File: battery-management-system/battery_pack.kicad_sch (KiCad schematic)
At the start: 15 parts, among them J1 Conn_01x01, J2 Conn_01x01, J3 Conn_01x01, J4 Conn_01x01, J5 Conn_01x01, J6 Conn_01x01, Q1 DMN3730U, Q2 TJ40S04M3L, Q3 TJ40S04M3L, Q4 DMN3730U

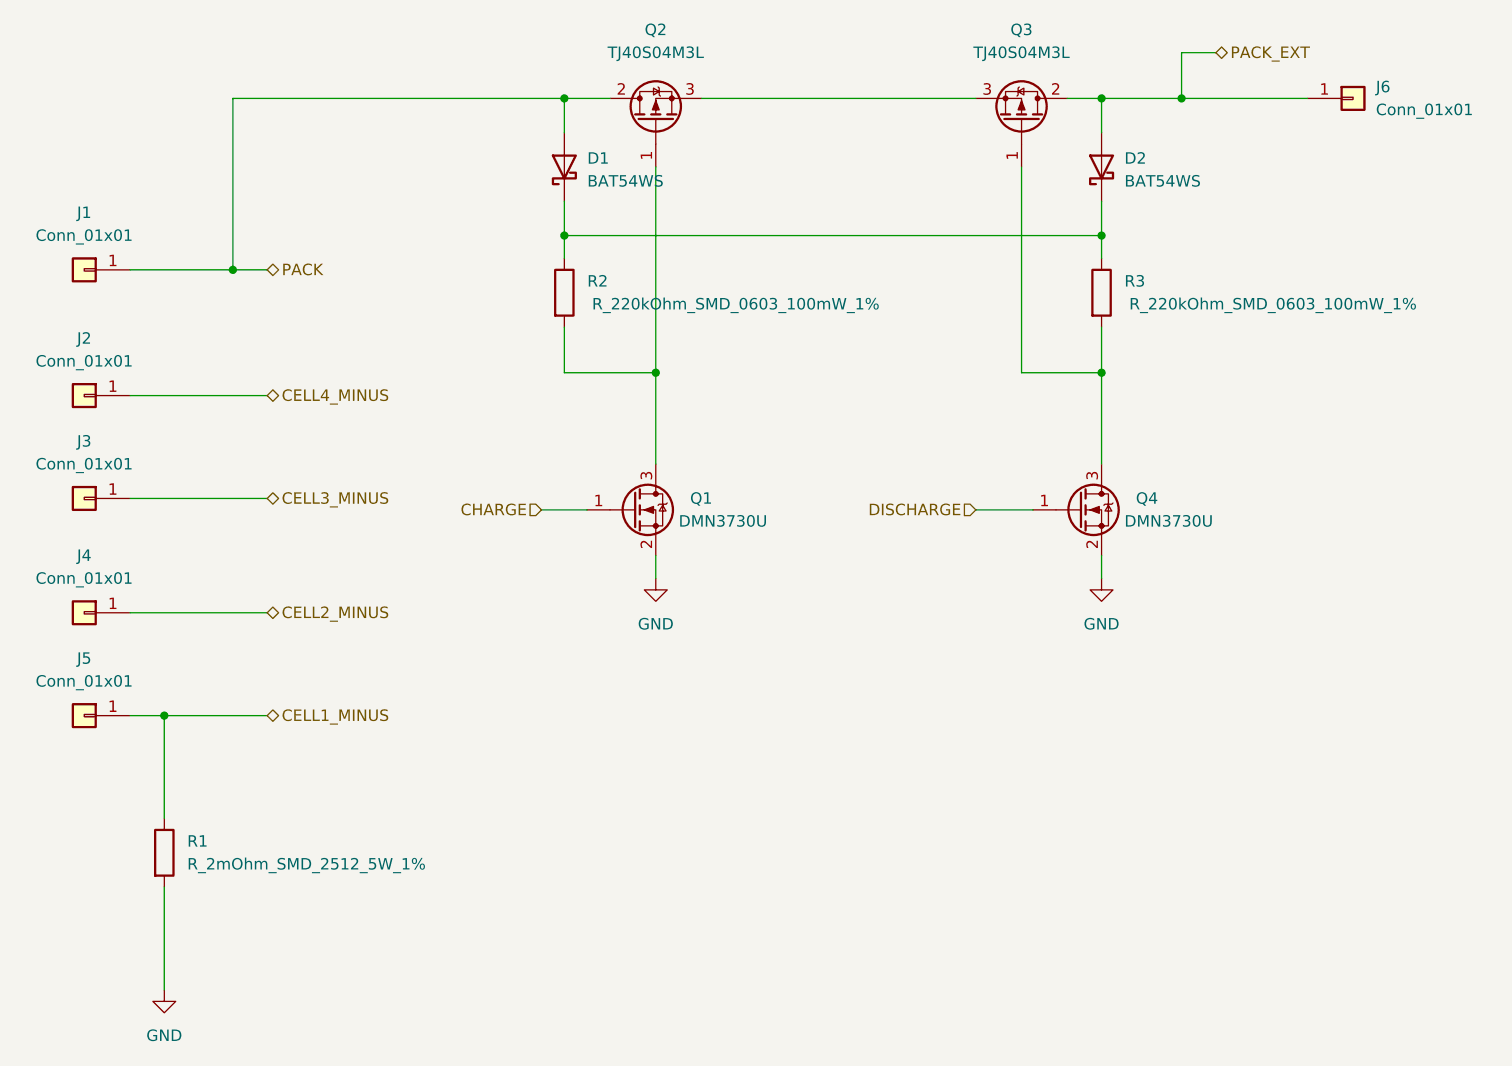
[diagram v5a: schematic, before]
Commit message: use M6 connectors, update symbols
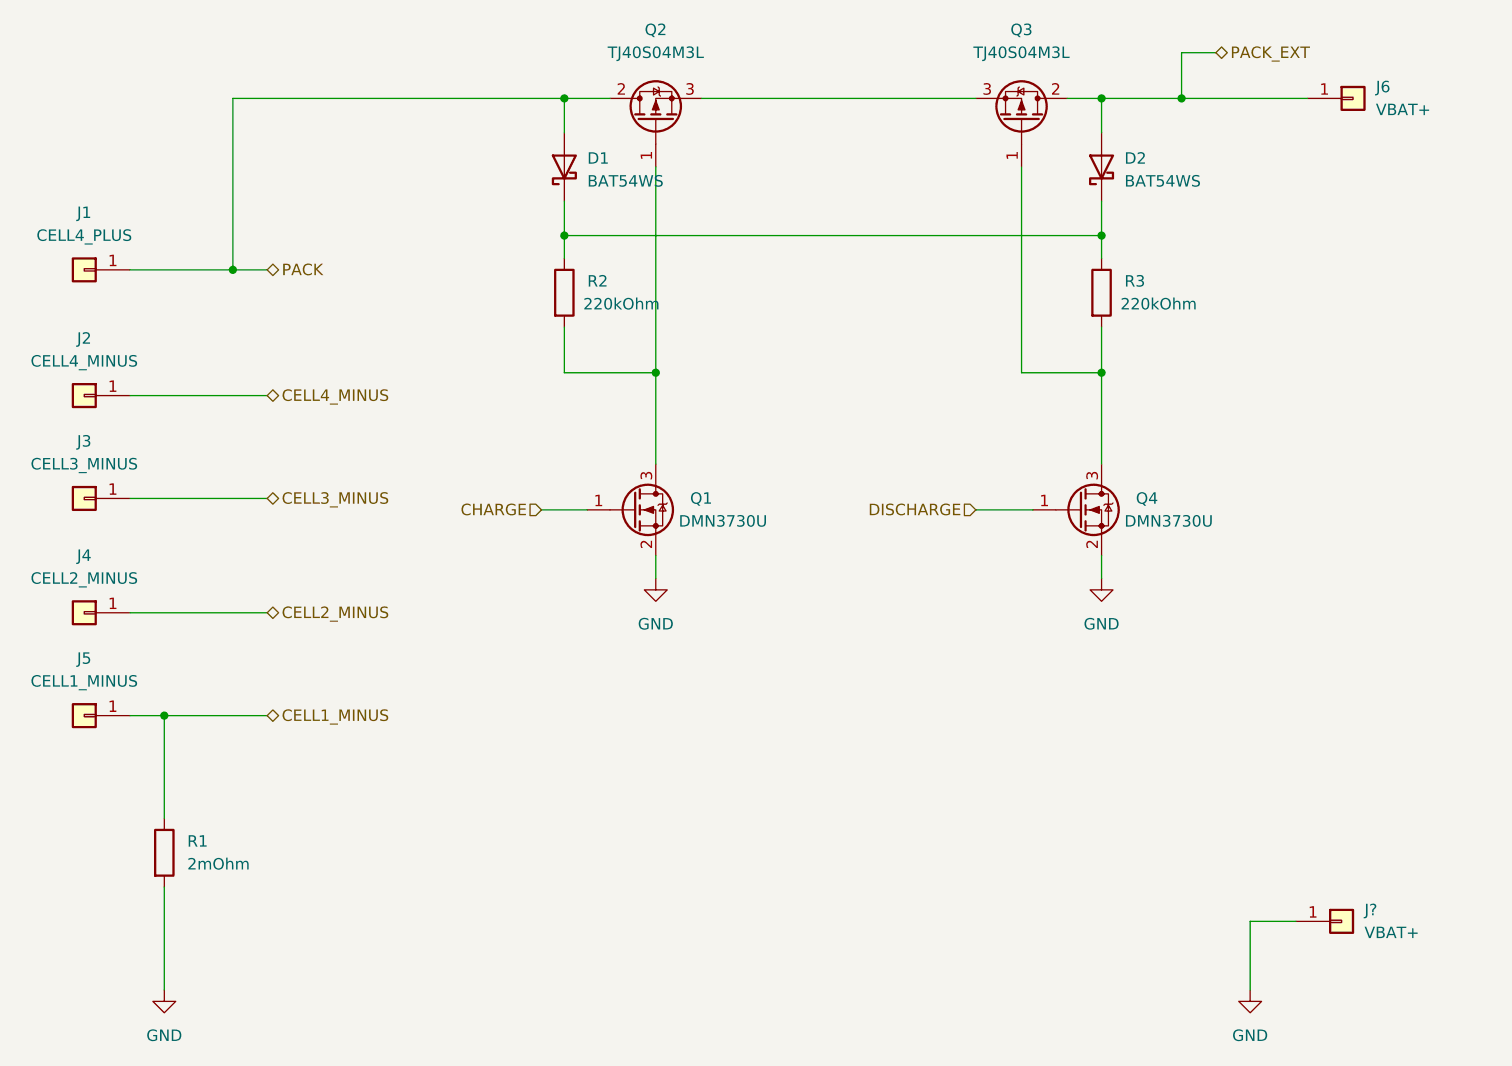
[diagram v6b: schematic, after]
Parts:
- added J?: VBAT+, benediktibk:Connector_M6, symbol benediktibk:Connector_M6
- J1: value Conn_01x01 -> CELL4_PLUS; footprint (none) -> benediktibk:Connector_M6; symbol Connector_Generic:Conn_01x01 -> benediktibk:Connector_M6
- J2: value Conn_01x01 -> CELL4_MINUS; footprint (none) -> benediktibk:Connector_M6; symbol Connector_Generic:Conn_01x01 -> benediktibk:Connector_M6
- J3: value Conn_01x01 -> CELL3_MINUS; footprint (none) -> benediktibk:Connector_M6; symbol Connector_Generic:Conn_01x01 -> benediktibk:Connector_M6
- J4: value Conn_01x01 -> CELL2_MINUS; footprint (none) -> benediktibk:Connector_M6; symbol Connector_Generic:Conn_01x01 -> benediktibk:Connector_M6
- J5: value Conn_01x01 -> CELL1_MINUS; footprint (none) -> benediktibk:Connector_M6; symbol Connector_Generic:Conn_01x01 -> benediktibk:Connector_M6
- J6: value Conn_01x01 -> VBAT+; footprint (none) -> benediktibk:Connector_M6; symbol Connector_Generic:Conn_01x01 -> benediktibk:Connector_M6
- R1: value R_2mOhm_SMD_2512_5W_1% -> 2mOhm; RS order number 231-3683 -> 231-3683
- R2, R3: value R_220kOhm_SMD_0603_100mW_1% -> 220kOhm
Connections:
- net GND: now also J?.1 (Pin_1)
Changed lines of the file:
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@@
+    (stroke (width 0) (type default) (color 0 0 0 0))
+  )
+  (wire (pts (xy 195.58 137.16) (xy 200.66 137.16))
     (stroke (width 0) (type default) (color 0 0 0 0))
   )
@@
   )
   (wire (pts (xy 74.93 114.3) (xy 74.93 125.73))
+    (stroke (width 0) (type default) (color 0 0 0 0))
+  )
+  (wire (pts (xy 195.58 144.78) (xy 195.58 137.16))
     (stroke (width 0) (type default) (color 0 0 0 0))
   )
@@
     (pin "2")
   )
-  (symbol (lib_id "Connector_Generic:Conn_01x01") (at 207.01 45.72 0) (unit 1)
+  (symbol (lib_id "benediktibk:Connector_M6") (at 205.74 137.16 0) (unit 1)
+    (in_bom yes) (on_board yes) (fields_autoplaced)
+    (property "Reference" "J?" (id 0) (at 208.28 135.8899 0)
+      (effects (font (size 1.27 1.27)) (justify left))
+    )
+    (property "Value" "VBAT+" (id 1) (at 208.28 138.4299 0)
+      (effects (font (size 1.27 1.27)) (justify left))
+    )
+    (property "Footprint" "benediktibk:Connector_M6" (id 2) (at 205.994 133.096 0)
+      (effects (font (size 1.27 1.27)) hide)
+    )
+    (property "Datasheet" "~" (id 3) (at 205.74 137.16 0)
+      (effects (font (size 1.27 1.27)) hide)
+    )
+    (property "RS order number" "" (id 4) (at 205.74 137.16 0)
+      (effects (font (size 1.27 1.27)) hide)
+    )
+    (pin "1")
+  )
+  (symbol (lib_id "benediktibk:Connector_M6") (at 207.01 45.72 0) (unit 1)
     (in_bom yes) (on_board yes) (fields_autoplaced)
     (property "Reference" "J6" (id 0) (at 209.55 44.4499 0)
       (effects (font (size 1.27 1.27)) (justify left))
     )
-    (property "Value" "Conn_01x01" (id 1) (at 209.55 46.9899 0)
-      (effects (font (size 1.27 1.27)) (justify left))
-    )
-    (property "Footprint" "" (id 2) (at 207.01 45.72 0)
+    (property "Value" "VBAT+" (id 1) (at 209.55 46.9899 0)
+      (effects (font (size 1.27 1.27)) (justify left))
+    )
+    (property "Footprint" "benediktibk:Connector_M6" (id 2) (at 207.264 41.656 0)
       (effects (font (size 1.27 1.27)) hide)
     )
@@
       (effects (font (size 1.27 1.27)) hide)
     )
-    (pin "1")
-  )
-  (symbol (lib_id "Connector_Generic:Conn_01x01") (at 66.04 90.17 0) (mirror y) (unit 1)
+    (property "RS order number" "" (id 4) (at 207.01 45.72 0)
+      (effects (font (size 1.27 1.27)) hide)
+    )
+    (pin "1")
+  )
+  (symbol (lib_id "benediktibk:Connector_M6") (at 66.04 90.17 0) (mirror y) (unit 1)
     (in_bom yes) (on_board yes) (fields_autoplaced)
     (property "Reference" "J3" (id 0) (at 66.04 83.82 0))
-    (property "Value" "Conn_01x01" (id 1) (at 66.04 86.36 0))
-    (property "Footprint" "" (id 2) (at 66.04 90.17 0)
+    (property "Value" "CELL3_MINUS" (id 1) (at 66.04 86.36 0))
+    (property "Footprint" "benediktibk:Connector_M6" (id 2) (at 65.786 86.106 0)
       (effects (font (size 1.27 1.27)) hide)
     )
     (property "Datasheet" "~" (id 3) (at 66.04 90.17 0)
+      (effects (font (size 1.27 1.27)) hide)
+    )
+    (property "RS order number" "" (id 4) (at 66.04 90.17 0)
       (effects (font (size 1.27 1.27)) hide)
     )
@@
       (effects (font (size 1.27 1.27)) (justify left))
     )
-    (property "Value" "R_220kOhm_SMD_0603_100mW_1%" (id 1) (at 138.43 68.58 0))
+    (property "Value" "220kOhm" (id 1) (at 125.73 68.58 0))
     (property "Footprint" "benediktibk:R_0603_1608Metric_Pad0.98x0.95mm_HandSolder" (id 2) (at 109.22 66.802 90)
       (effects (font (size 1.27 1.27)) hide)
@@
       (effects (font (size 1.27 1.27)) (justify left))
     )
-    (property "Value" "R_2mOhm_SMD_2512_5W_1%" (id 1) (at 77.47 130.8099 0)
+    (property "Value" "2mOhm" (id 1) (at 77.47 130.8099 0)
       (effects (font (size 1.27 1.27)) (justify left))
     )
@@
       (effects (font (size 1.27 1.27)) hide)
     )
-    (property "RS order number" "    231-3683" (id 4) (at 57.15 128.27 0)
+    (property "RS order number" "231-3683" (id 4) (at 57.15 128.27 0)
       (effects (font (size 1.27 1.27)) hide)
     )
@@
       (effects (font (size 1.27 1.27)) (justify left))
     )
-    (property "Value" "R_220kOhm_SMD_0603_100mW_1%" (id 1) (at 198.12 68.58 0))
+    (property "Value" "220kOhm" (id 1) (at 185.42 68.58 0))
     (property "Footprint" "benediktibk:R_0603_1608Metric_Pad0.98x0.95mm_HandSolder" (id 2) (at 168.91 66.802 90)
       (effects (font (size 1.27 1.27)) hide)
@@
     (pin "3")
   )
-  (symbol (lib_id "Connector_Generic:Conn_01x01") (at 66.04 64.77 0) (mirror y) (unit 1)
+  (symbol (lib_id "benediktibk:Connector_M6") (at 66.04 64.77 0) (mirror y) (unit 1)
     (in_bom yes) (on_board yes) (fields_autoplaced)
     (property "Reference" "J1" (id 0) (at 66.04 58.42 0))
-    (property "Value" "Conn_01x01" (id 1) (at 66.04 60.96 0))
-    (property "Footprint" "" (id 2) (at 66.04 64.77 0)
+    (property "Value" "CELL4_PLUS" (id 1) (at 66.04 60.96 0))
+    (property "Footprint" "benediktibk:Connector_M6" (id 2) (at 65.786 60.706 0)
       (effects (font (size 1.27 1.27)) hide)
     )
@@
       (effects (font (size 1.27 1.27)) hide)
     )
-    (pin "1")
-  )
-  (symbol (lib_id "Connector_Generic:Conn_01x01") (at 66.04 114.3 0) (mirror y) (unit 1)
+    (property "RS order number" "" (id 4) (at 66.04 64.77 0)
+      (effects (font (size 1.27 1.27)) hide)
+    )
+    (pin "1")
+  )
+  (symbol (lib_id "benediktibk:Connector_M6") (at 66.04 114.3 0) (mirror y) (unit 1)
     (in_bom yes) (on_board yes) (fields_autoplaced)
     (property "Reference" "J5" (id 0) (at 66.04 107.95 0))
-    (property "Value" "Conn_01x01" (id 1) (at 66.04 110.49 0))
-    (property "Footprint" "" (id 2) (at 66.04 114.3 0)
+    (property "Value" "CELL1_MINUS" (id 1) (at 66.04 110.49 0))
+    (property "Footprint" "benediktibk:Connector_M6" (id 2) (at 65.786 110.236 0)
       (effects (font (size 1.27 1.27)) hide)
     )
     (property "Datasheet" "~" (id 3) (at 66.04 114.3 0)
+      (effects (font (size 1.27 1.27)) hide)
+    )
+    (property "RS order number" "" (id 4) (at 66.04 114.3 0)
       (effects (font (size 1.27 1.27)) hide)
     )
@@
     (pin "2")
   )
-  (symbol (lib_id "Connector_Generic:Conn_01x01") (at 66.04 78.74 0) (mirror y) (unit 1)
+  (symbol (lib_id "benediktibk:Connector_M6") (at 66.04 78.74 0) (mirror y) (unit 1)
     (in_bom yes) (on_board yes) (fields_autoplaced)
     (property "Reference" "J2" (id 0) (at 66.04 72.39 0))
-    (property "Value" "Conn_01x01" (id 1) (at 66.04 74.93 0))
-    (property "Footprint" "" (id 2) (at 66.04 78.74 0)
+    (property "Value" "CELL4_MINUS" (id 1) (at 66.04 74.93 0))
+    (property "Footprint" "benediktibk:Connector_M6" (id 2) (at 65.786 74.676 0)
       (effects (font (size 1.27 1.27)) hide)
     )
@@
       (effects (font (size 1.27 1.27)) hide)
     )
-    (pin "1")
-  )
-  (symbol (lib_id "Connector_Generic:Conn_01x01") (at 66.04 102.87 0) (mirror y) (unit 1)
+    (property "RS order number" "" (id 4) (at 66.04 78.74 0)
+      (effects (font (size 1.27 1.27)) hide)
+    )
+    (pin "1")
+  )
+  (symbol (lib_id "power:GND") (at 195.58 144.78 0) (unit 1)
+    (in_bom yes) (on_board yes) (fields_autoplaced)
+    (property "Reference" "#PWR?" (id 0) (at 195.58 151.13 0)
+      (effects (font (size 1.27 1.27)) hide)
+    )
+    (property "Value" "GND" (id 1) (at 195.58 149.86 0))
+    (property "Footprint" "" (id 2) (at 195.58 144.78 0)
+      (effects (font (size 1.27 1.27)) hide)
+    )
+    (property "Datasheet" "" (id 3) (at 195.58 144.78 0)
+      (effects (font (size 1.27 1.27)) hide)
+    )
+    (pin "1")
+  )
+  (symbol (lib_id "benediktibk:Connector_M6") (at 66.04 102.87 0) (mirror y) (unit 1)
     (in_bom yes) (on_board yes) (fields_autoplaced)
     (property "Reference" "J4" (id 0) (at 66.04 96.52 0))
-    (property "Value" "Conn_01x01" (id 1) (at 66.04 99.06 0))
-    (property "Footprint" "" (id 2) (at 66.04 102.87 0)
+    (property "Value" "CELL2_MINUS" (id 1) (at 66.04 99.06 0))
+    (property "Footprint" "benediktibk:Connector_M6" (id 2) (at 65.786 98.806 0)
       (effects (font (size 1.27 1.27)) hide)
     )
@@
       (effects (font (size 1.27 1.27)) hide)
     )
+    (property "RS order number" "" (id 4) (at 66.04 102.87 0)
+      (effects (font (size 1.27 1.27)) hide)
+    )

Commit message: update PCB
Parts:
- gave numbers to parts that had none: 1
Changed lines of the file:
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@@
   (symbol (lib_id "benediktibk:Connector_M6") (at 205.74 137.16 0) (unit 1)
     (in_bom yes) (on_board yes) (fields_autoplaced)
-    (property "Reference" "J?" (id 0) (at 208.28 135.8899 0)
+    (property "Reference" "J8" (id 0) (at 208.28 135.8899 0)
       (effects (font (size 1.27 1.27)) (justify left))
     )
@@
   (symbol (lib_id "power:GND") (at 195.58 144.78 0) (unit 1)
     (in_bom yes) (on_board yes) (fields_autoplaced)
-    (property "Reference" "#PWR?" (id 0) (at 195.58 151.13 0)
-      (effects (font (size 1.27 1.27)) hide)
-    )
+    (property "Reference" "#PWR0116" (id 0) (at 195.58 151.13 0)
+      (effects (font (size 1.27 1.27)) hide)
+    )
